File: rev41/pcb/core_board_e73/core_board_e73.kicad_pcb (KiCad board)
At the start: 2 copper layers, 43.2 x 54 mm, 53 parts, among them J1 USB_C_Receptacle_USB2.0_16P, J2 Conn_02x10_Odd_Even, J3 Conn_02x10_Odd_Even, J4 USB_C_Receptacle_USB2.0_16P, J5 Conn_01x08_MountingPin, J6 Conn_01x08_MountingPin, J7 Debug, J8 Conn_Batt, J9 USB_C_Receptacle_USB2.0_16P, SW1 SW_SPDT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

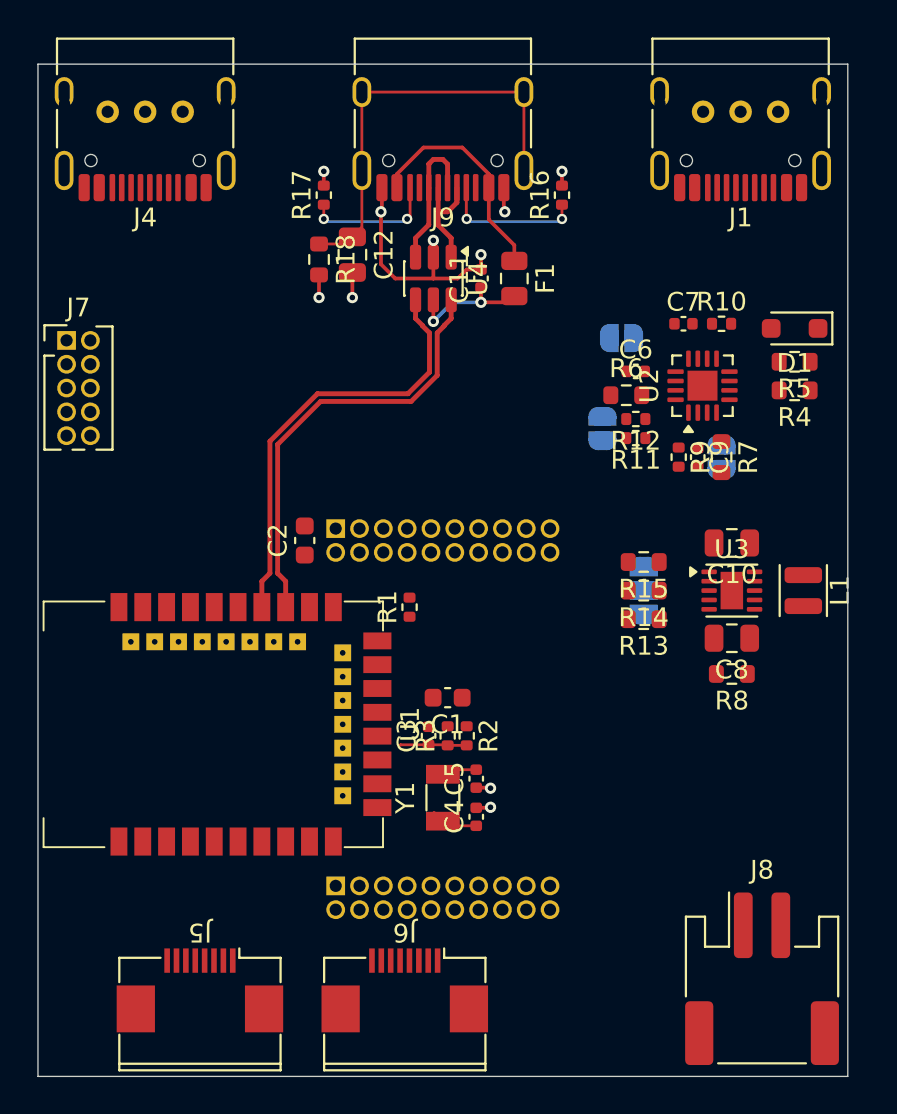
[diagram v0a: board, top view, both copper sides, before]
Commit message: feat: core board e73 basic routed
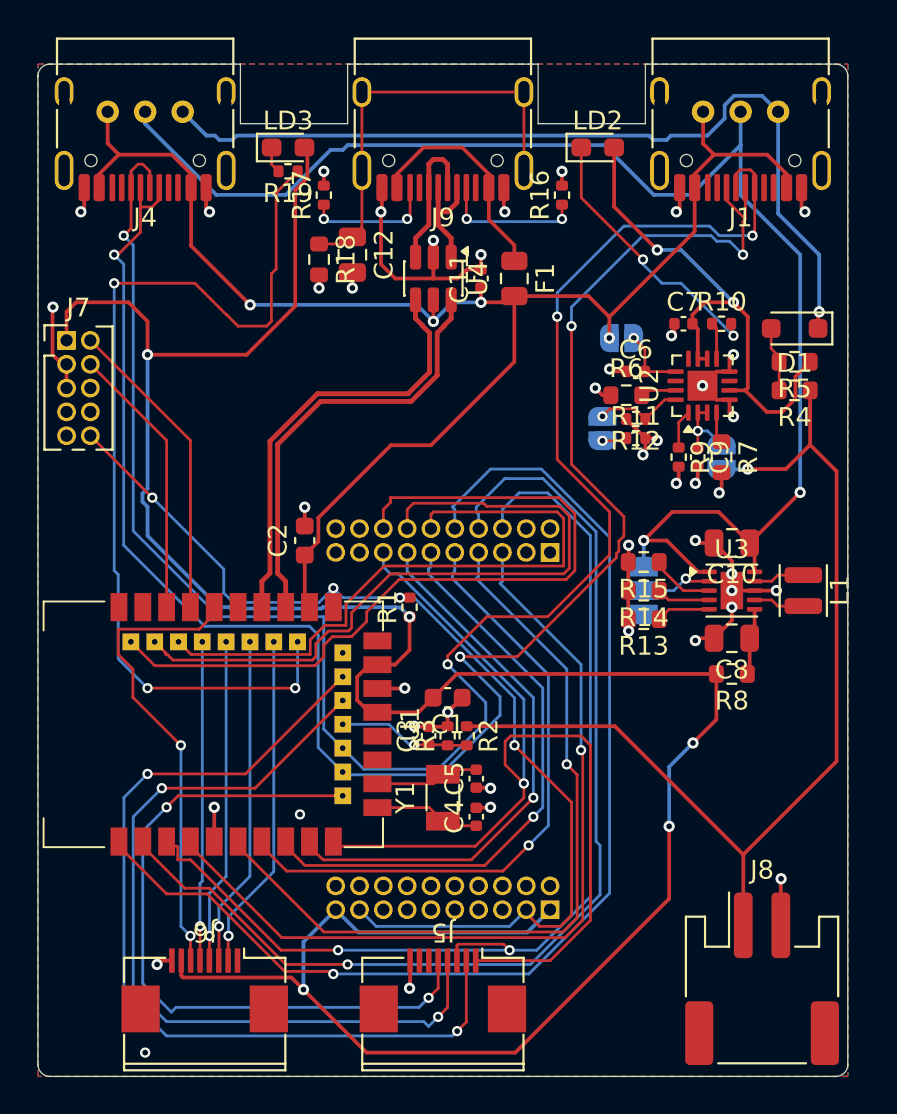
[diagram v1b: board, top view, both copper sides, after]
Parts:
- added LD2: LED, LED_SMD:LED_0603_1608Metric_Pad1.05x0.95mm_HandSolder, F.Cu at (160.7, 52.7)
- added LD3: LED, LED_SMD:LED_0603_1608Metric_Pad1.05x0.95mm_HandSolder, F.Cu at (144.1, 52.7)
- added R19: 10k, Resistor_SMD:R_0402_1005Metric, F.Cu at (144.1, 54.0)
- J6: value Conn_01x08_MountingPin -> Conn_MouseSensor
- moved J5 13.0 mm to (152.4, 99.1)
- moved J2 11.5 mm to (158.1, 74.3), turned to 90 degrees
- moved J3 11.5 mm to (158.1, 93.3), turned to 90 degrees
- moved J6 10.7 mm to (139.7, 99.1)
- turned R11 to 0 degrees
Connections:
- J2 pad 10: unconnected-(J2-Pin_10-Pad10) -> COL_2
- J2 pad 11: unconnected-(J2-Pin_11-Pad11) -> ROW_3
- J2 pad 12: unconnected-(J2-Pin_12-Pad12) -> COL_3
- J2 pad 13: unconnected-(J2-Pin_13-Pad13) -> ROW_4
- J2 pad 14: unconnected-(J2-Pin_14-Pad14) -> COL_4
- J2 pad 15: unconnected-(J2-Pin_15-Pad15) -> ROW_5
- J2 pad 16: unconnected-(J2-Pin_16-Pad16) -> COL_5
- J2 pad 5: unconnected-(J2-Pin_5-Pad5) -> ROW_0
- J2 pad 6: unconnected-(J2-Pin_6-Pad6) -> COL_0
- J2 pad 7: unconnected-(J2-Pin_7-Pad7) -> ROW_1
- J2 pad 8: unconnected-(J2-Pin_8-Pad8) -> COL_1
- J2 pad 9: unconnected-(J2-Pin_9-Pad9) -> ROW_2
- J5 pad 1: unconnected-(J5-Pin_1-Pad1) -> ROW_5
- J5 pad 2: unconnected-(J5-Pin_2-Pad2) -> ROW_6
- J5 pad 3: unconnected-(J5-Pin_3-Pad3) -> COL_0
- J5 pad 4: unconnected-(J5-Pin_4-Pad4) -> COL_6
- J5 pad 5: unconnected-(J5-Pin_5-Pad5) -> COL_7
- J5 pad 8: unconnected-(J5-Pin_8-Pad8) -> GND
- J6 pad 2: unconnected-(J6-Pin_2-Pad2) -> MOTION
- J6 pad 3: unconnected-(J6-Pin_3-Pad3) -> SCLK
- J6 pad 4: unconnected-(J6-Pin_4-Pad4) -> MOSI
- J6 pad 5: unconnected-(J6-Pin_5-Pad5) -> MISO
- J6 pad 6: unconnected-(J6-Pin_6-Pad6) -> nCS
- J6 pad 7: unconnected-(J6-Pin_7-Pad7) -> VDD
- J6 pad 8: unconnected-(J6-Pin_8-Pad8) -> GND
- U1 pad 1: unconnected-(U1-P1.11-Pad1) -> COL_2
- U1 pad 10: unconnected-(U1-P0.30-Pad10) -> ROW_5
- U1 pad 12: unconnected-(U1-P0.26-Pad12) -> COL_7
- U1 pad 2: unconnected-(U1-P1.10-Pad2) -> COL_1
- U1 pad 20: unconnected-(U1-P0.12-Pad20) -> COL_6
- U1 pad 22: unconnected-(U1-P0.07-Pad22) -> ROW_6
- U1 pad 28: unconnected-(U1-P0.15-Pad28) -> Net-(U1-P0.15)
- U1 pad 3: unconnected-(U1-P0.03-Pad3) -> COL_0
- U1 pad 30: unconnected-(U1-P0.17-Pad30) -> MOTION
- U1 pad 32: unconnected-(U1-P0.20-Pad32) -> SCLK
- U1 pad 34: unconnected-(U1-P0.22-Pad34) -> MOSI
- U1 pad 35: unconnected-(U1-P0.24-Pad35) -> nCS
- U1 pad 36: unconnected-(U1-P1.00-Pad36) -> MISO
- U1 pad 38: unconnected-(U1-P1.02-Pad38) -> COL_3
- U1 pad 4: unconnected-(U1-P0.28-Pad4) -> ROW_0
- U1 pad 40: unconnected-(U1-P1.04-Pad40) -> COL_4
- U1 pad 42: unconnected-(U1-P1.06-Pad42) -> COL_5
- U1 pad 6: unconnected-(U1-P1.13-Pad6) -> ROW_1
- U1 pad 7: unconnected-(U1-P0.02-Pad7) -> ROW_2
- U1 pad 8: unconnected-(U1-P0.29-Pad8) -> ROW_3
- U1 pad 9: unconnected-(U1-P0.31-Pad9) -> ROW_4
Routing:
- net VDD: track 0.00 -> 140.7 mm, vias 0 -> 5
- net RX: track 0.00 -> 98.0 mm, vias 0 -> 4
- net TX: track 0.00 -> 97.8 mm, vias 0 -> 4
- net /power/VIN_DCDC: track 0.00 -> 76.8 mm, vias 0 -> 2
- net VBUS: track 6.82 -> 81.7 mm, vias 2 -> 4
- net COL_2: track 0.00 -> 61.7 mm, vias 0 -> 1
- net COL_1: track 0.00 -> 57.4 mm, vias 0 -> 1
- net RESET: track 0.00 -> 56.7 mm, vias 0 -> 4
- net COL_0: track 0.00 -> 56.5 mm, vias 0 -> 2
- net +BATT: track 0.00 -> 54.0 mm, vias 0 -> 1
- net GND: track 19.7 -> 71.6 mm, vias 10 -> 44
- net ROW_5: track 0.00 -> 51.5 mm, vias 0 -> 1
- net Net-(U1-P0.15): track 0.00 -> 50.7 mm, vias 0 -> 3
- net ROW_6: track 0.00 -> 47.6 mm, vias 0 -> 2
- net /power/VBATT_SRC: track 0.00 -> 46.8 mm, vias 0 -> 1
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- added copper zone on B.Cu, net GND
- added copper zone on F.Cu, net GND
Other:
- outline, holes or cut-outs redrawn

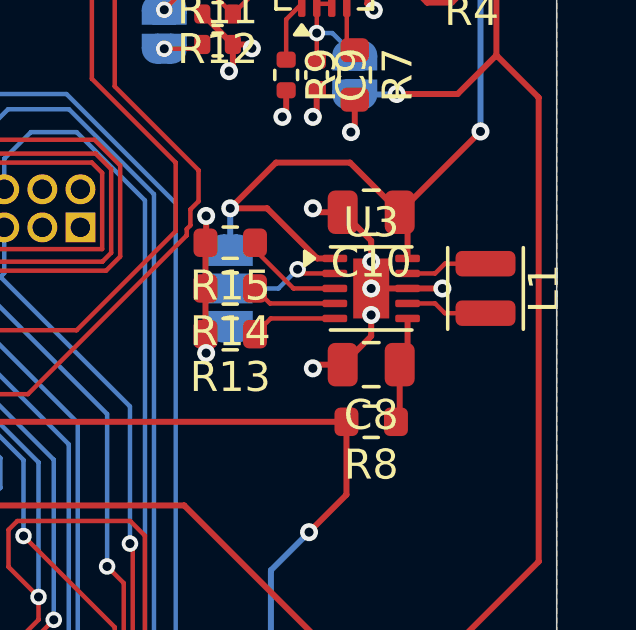
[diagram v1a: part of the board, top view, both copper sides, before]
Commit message: feat: add DCDC zone
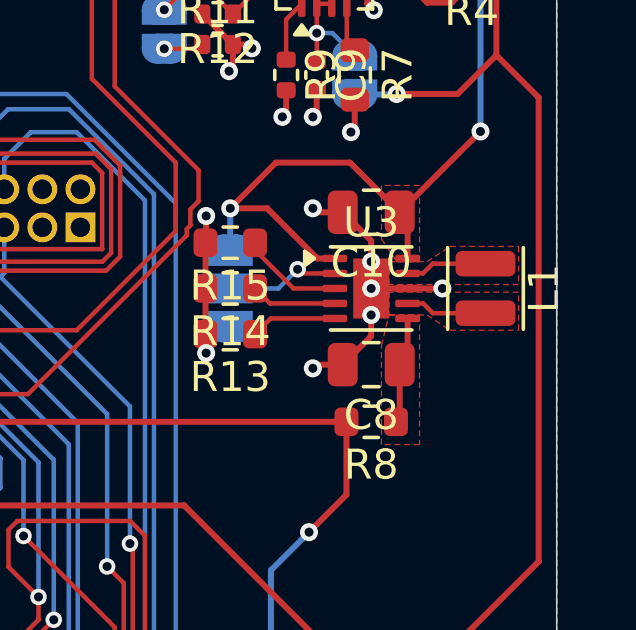
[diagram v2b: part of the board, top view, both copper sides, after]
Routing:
- added copper zone on F.Cu, net /power/VIN_DCDC
- added copper zone on F.Cu, net Net-(U3-LX1)
- added copper zone on F.Cu, net Net-(U3-LX2)
- added copper zone on F.Cu, net Net-(U3-VOUT)
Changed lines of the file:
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@@
 	)
 	(segment
-		(start 167.8075 76.331)
-		(end 167.8075 74.741)
-		(width 0.2)
-		(layer "F.Cu")
-		(net "GND")
-	)
-	(segment
 		(start 163.703 68.199)
 		(end 163.83 68.326)
@@
 	)
 	(segment
-		(start 167.8075 74.741)
-		(end 166.8575 73.791)
+		(start 167.8075 76.331)
+		(end 167.8075 74.741)
 		(width 0.2)
 		(layer "F.Cu")
@@
 	)
 	(segment
+		(start 167.8075 74.741)
+		(end 166.8575 73.791)
+		(width 0.2)
+		(layer "F.Cu")
+		(net "GND")
+	)
+	(segment
 		(start 165.985 78.871)
 		(end 165.862 78.994)
@@
 	)
 	(segment
-		(start 169.937537 75.831)
-		(end 170.262537 75.506)
+		(start 169.533 75.831)
+		(end 169.858 75.506)
 		(width 0.15)
 		(layer "F.Cu")
@@
 	)
 	(segment
-		(start 170.262537 75.506)
-		(end 171.6175 75.506)
+		(start 169.02 75.831)
+		(end 169.533 75.831)
 		(width 0.15)
 		(layer "F.Cu")
@@
 	)
 	(segment
-		(start 169.02 75.831)
-		(end 169.937537 75.831)
+		(start 169.858 75.506)
+		(end 171.6175 75.506)
 		(width 0.15)
 		(layer "F.Cu")
@@
 	)
 	(segment
-		(start 169.02 76.831)
-		(end 169.937537 76.831)
+		(start 169.866 77.156)
+		(end 171.6175 77.156)
 		(width 0.15)
 		(layer "F.Cu")
@@
 	)
 	(segment
-		(start 169.937537 76.831)
-		(end 170.262537 77.156)
+		(start 169.02 76.831)
+		(end 169.541 76.831)
 		(width 0.15)
 		(layer "F.Cu")
@@
 	)
 	(segment
-		(start 170.262537 77.156)
-		(end 171.6175 77.156)
+		(start 169.541 76.831)
+		(end 169.866 77.156)
 		(width 0.15)
 		(layer "F.Cu")
@@
 	)
 	(zone
+		(net "/power/VIN_DCDC")
+		(layer "F.Cu")
+		(name "DCDCLVI")
+		(hatch edge 0.5)
+		(priority 3)
+		(connect_pads yes
+			(clearance 0.25)
+		)
+		(min_thickness 0.25)
+		(fill yes
+			(thermal_gap 0.25)
+			(thermal_bridge_width 0.25)
+			(island_removal_mode 0)
+		)
+		(polygon
+			(pts
+				(xy 169.418 75.438) (xy 169.418 72.898) (xy 168.148 72.898) (xy 168.148 74.676) (xy 168.656 75.438)
+			)
+		)
+	)
+	(zone
+		(net "Net-(U3-VOUT)")
+		(layer "F.Cu")
+		(name "DCDCVO")
+		(hatch edge 0.5)
+		(priority 2)
+		(connect_pads yes
+			(clearance 0.25)
+		)
+		(min_thickness 0.25)
+		(fill yes
+			(thermal_gap 0.25)
+			(thermal_bridge_width 0.25)
+			(island_removal_mode 0)
+		)
+		(polygon
+			(pts
+				(xy 168.402 77.216) (xy 169.418 77.216) (xy 169.418 81.534) (xy 168.148 81.534) (xy 168.148 78.232)
+			)
+		)
+	)
+	(zone
+		(net "Net-(U3-LX1)")
+		(layer "F.Cu")
+		(name "DCDCL1")
+		(hatch edge 0.5)
+		(priority 1)
+		(connect_pads yes
+			(clearance 0.25)
+		)
+		(min_thickness 0.25)
+		(fill yes
+			(thermal_gap 0.25)
+			(thermal_bridge_width 0.25)
+			(island_removal_mode 0)
+		)
+		(polygon
+			(pts
+				(xy 168.402 75.438) (xy 169.672 75.438) (xy 170.434 74.93) (xy 172.72 74.93) (xy 172.72 76.2) (xy 168.402 76.2)
+			)
+		)
+	)
+	(zone
+		(net "Net-(U3-LX2)")
+		(layer "F.Cu")
+		(name "DCDCL1")
+		(hatch edge 0.5)
+		(priority 1)
+		(connect_pads yes
+			(clearance 0.25)
+		)
+		(min_thickness 0.25)
+		(fill yes
+			(thermal_gap 0.25)
+			(thermal_bridge_width 0.25)
+			(island_removal_mode 0)
+		)
+		(polygon
+			(pts
+				(xy 168.402 77.216) (xy 169.672 77.216) (xy 170.434 77.724) (xy 172.72 77.724) (xy 172.72 76.454)
+				(xy 168.402 76.454)
+			)
+		)
+	)
+	(zone
 		(layers "F.Cu" "B.Cu")
 		(name "an")
@@
 	(zone
 		(net "GND")
+		(locked yes)
 		(layers "F.Cu" "B.Cu")
 		(name "G1")

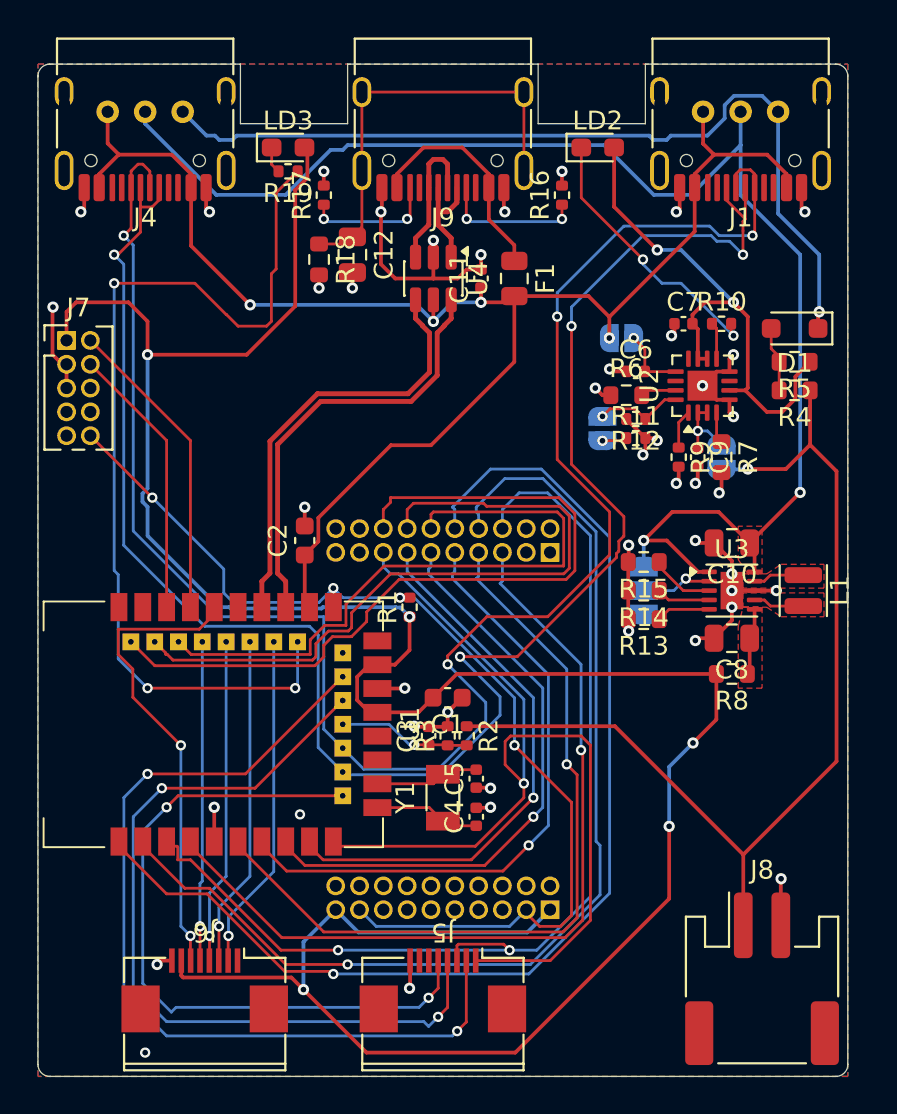
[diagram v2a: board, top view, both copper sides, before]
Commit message: feat: update silkscreen
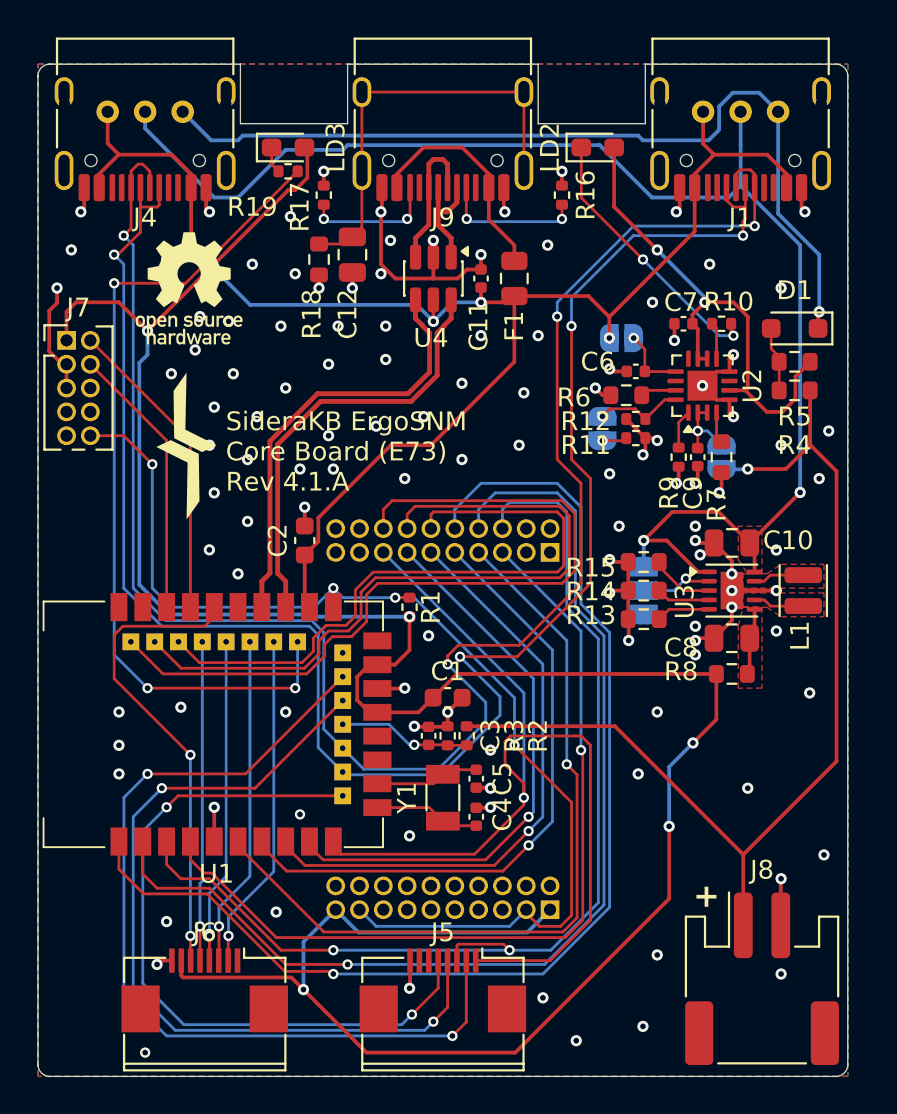
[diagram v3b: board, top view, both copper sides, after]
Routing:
- net Net-(U1-P0.15): track 50.7 -> 45.0 mm
- net RESET: track 56.7 -> 60.3 mm
- net GND: track 71.6 -> 74.7 mm, vias 44 -> 118
- net VDD: track 140.7 -> 138.1 mm
- net TX: track 97.8 -> 96.4 mm
- net VDDH: track 28.7 -> 27.3 mm
- net ROW_5: track 51.5 -> 52.6 mm
- net RX: track 98.0 -> 97.1 mm
- net COL_5: track 42.0 -> 42.6 mm
- net COL_1: track 57.4 -> 58.0 mm
- net COL_3: track 34.5 -> 35.1 mm
- net COL_7: track 38.0 -> 38.5 mm
- net COL_0: track 56.5 -> 57.0 mm
- net /power/VIN_DCDC: track 76.8 -> 76.3 mm
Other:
- board text added: "+"
- board text added: "CHG"
- board text added: "ON"
- board text added: "STA"
- board text added: "SideraKB ErgoSNM Core Board (E73) Rev ${REVISION}"

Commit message: feat: add thumb cluster
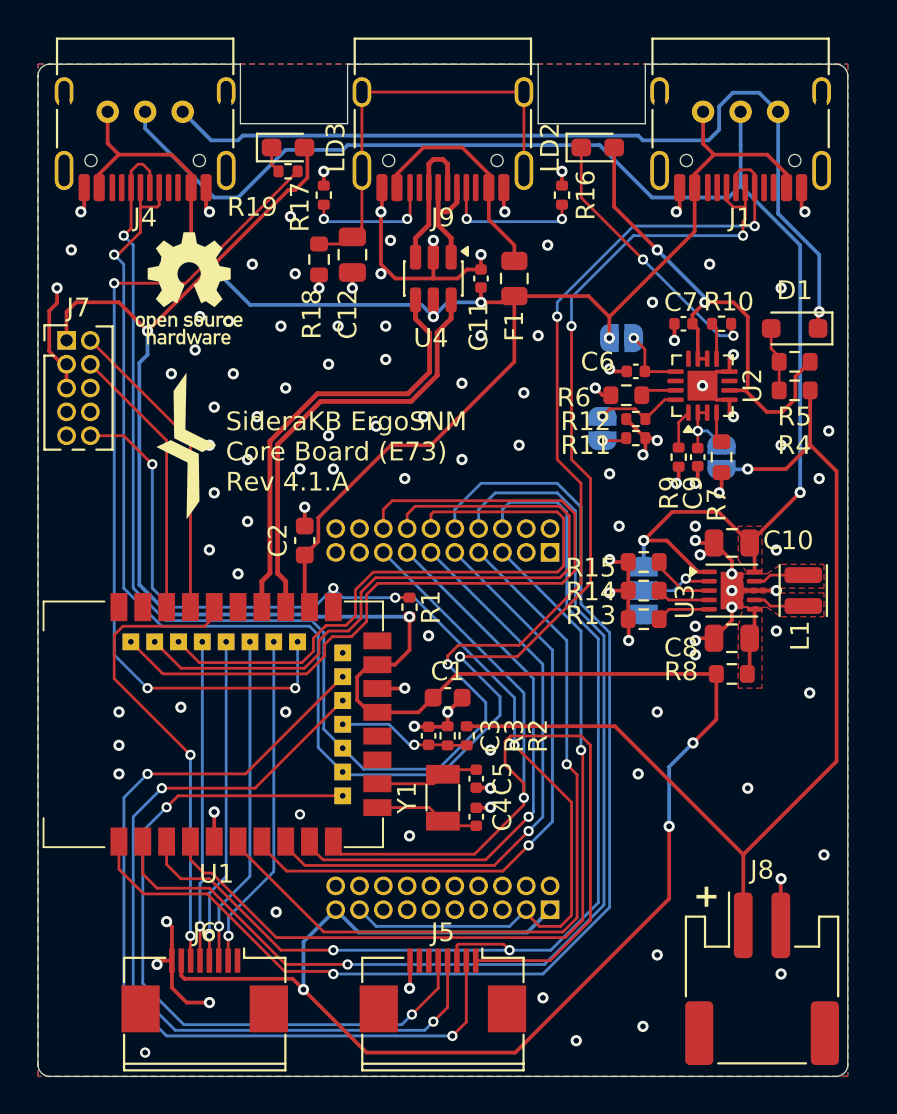
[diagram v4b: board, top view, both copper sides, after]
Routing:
- net GND: track 74.7 -> 80.5 mm, vias 118 -> 119
